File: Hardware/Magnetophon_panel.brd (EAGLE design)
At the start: 128.5 x 20 mm, 2 parts

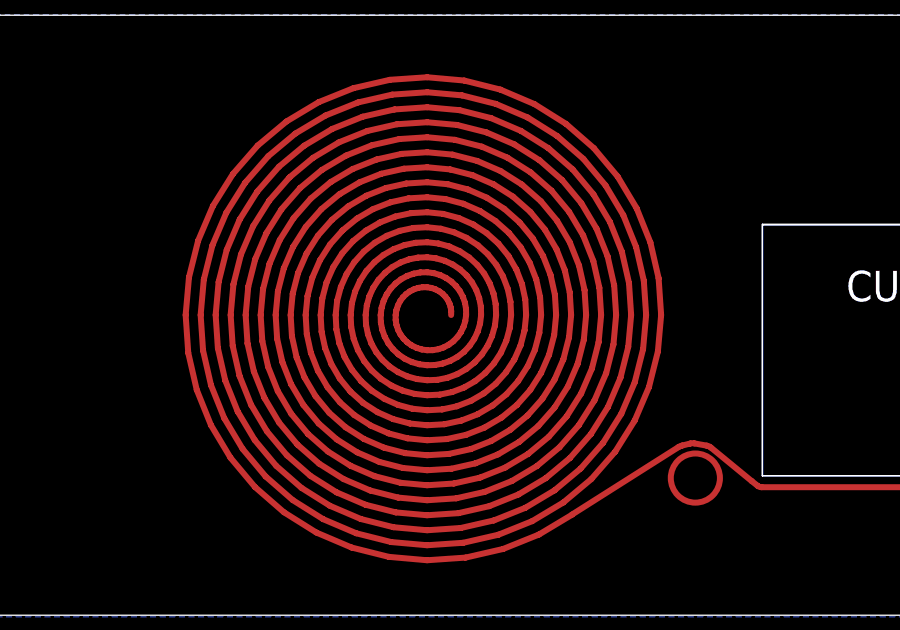
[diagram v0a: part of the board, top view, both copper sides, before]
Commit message: Add via to ground panel artwork
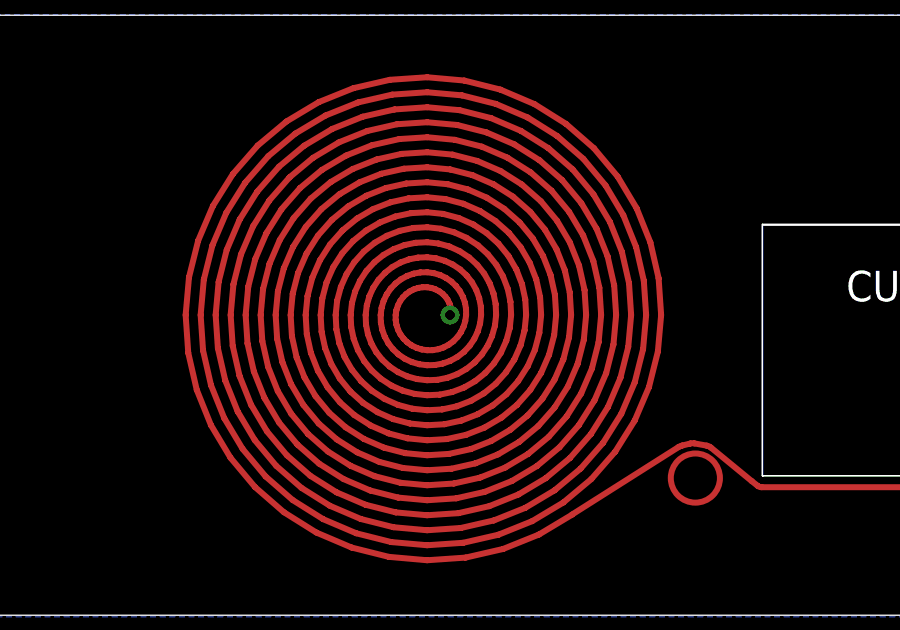
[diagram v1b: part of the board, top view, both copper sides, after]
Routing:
- net N$1: track 420.7 -> 0.00 mm
- net GND: track 0.00 -> 420.7 mm, vias 3 -> 4
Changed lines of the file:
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@@
 <?xml version="1.0" encoding="utf-8"?>
 <!DOCTYPE eagle SYSTEM "eagle.dtd">
-<eagle version="7.2.0">
+<eagle version="7.4.0">
 <drawing>
 <settings>
@@
 <setting verticaltext="up"/>
 </settings>
-<grid distance="2" unitdist="mil" unit="mm" style="lines" multiple="1" display="yes" altdistance="1" altunitdist="mil" altunit="mil"/>
+<grid distance="2" unitdist="mil" unit="mil" style="lines" multiple="1" display="yes" altdistance="1" altunitdist="mil" altunit="mil"/>
 <layers>
 <layer number="1" name="Top" color="4" fill="1" visible="yes" active="yes"/>
@@
 <layer number="14" name="Route14" color="1" fill="6" visible="no" active="no"/>
 <layer number="15" name="Route15" color="4" fill="6" visible="no" active="yes"/>
-<layer number="16" name="Bottom" color="1" fill="1" visible="no" active="yes"/>
+<layer number="16" name="Bottom" color="1" fill="1" visible="yes" active="yes"/>
 <layer number="17" name="Pads" color="2" fill="1" visible="yes" active="yes"/>
 <layer number="18" name="Vias" color="2" fill="1" visible="yes" active="yes"/>
-<layer number="19" name="Unrouted" color="6" fill="1" visible="no" active="yes"/>
+<layer number="19" name="Unrouted" color="6" fill="1" visible="yes" active="yes"/>
 <layer number="20" name="Dimension" color="15" fill="1" visible="yes" active="yes"/>
 <layer number="21" name="tPlace" color="7" fill="1" visible="no" active="yes"/>
@@
 <vertex x="0" y="-0.0508"/>
 </polygon>
-</signal>
-<signal name="N$1">
 <wire x1="77.5588" y1="10.0076" x2="77.5613" y2="10.1347" width="0.2" layer="1"/>
 <wire x1="77.5613" y1="10.1347" x2="77.5434" y2="10.2625" width="0.2" layer="1"/>
@@
 <wire x1="79.2927" y1="2.2089" x2="80.4872" y2="2.6902" width="0.2" layer="1"/>
 <wire x1="80.4872" y1="2.6902" x2="81.5933" y2="3.3534" width="0.2" layer="1"/>
+<via x="77.5208" y="10.0076" extent="1-16" drill="0.3302"/>
+<wire x1="77.5208" y1="10.0076" x2="77.5588" y2="10.0076" width="0" layer="19" extent="1-1"/>
 </signal>
 <signal name="N$2">
